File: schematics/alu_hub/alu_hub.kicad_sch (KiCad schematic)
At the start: 23 parts, among them U1 74LS574, U10 74LS02, U2 74LS245, U3 74LS02, U4 74LS181, U5 74LS181, U6 74LS574, U7 74LS245, U8 74LS245, U9 74LS02

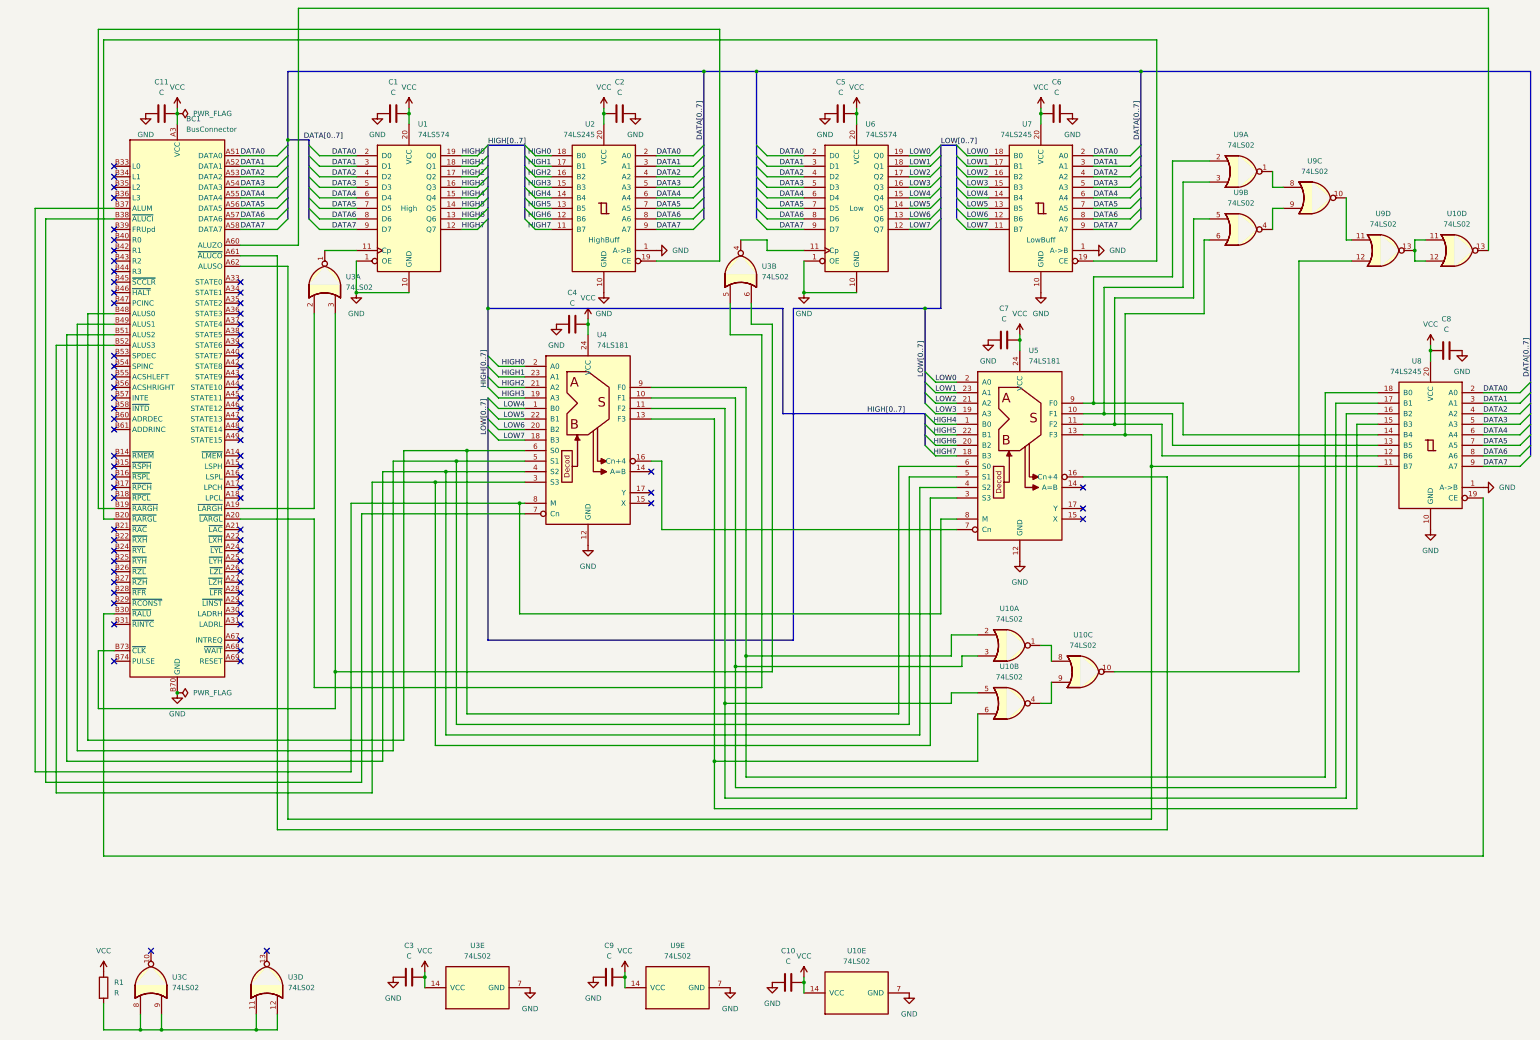
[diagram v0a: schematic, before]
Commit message: Add test points
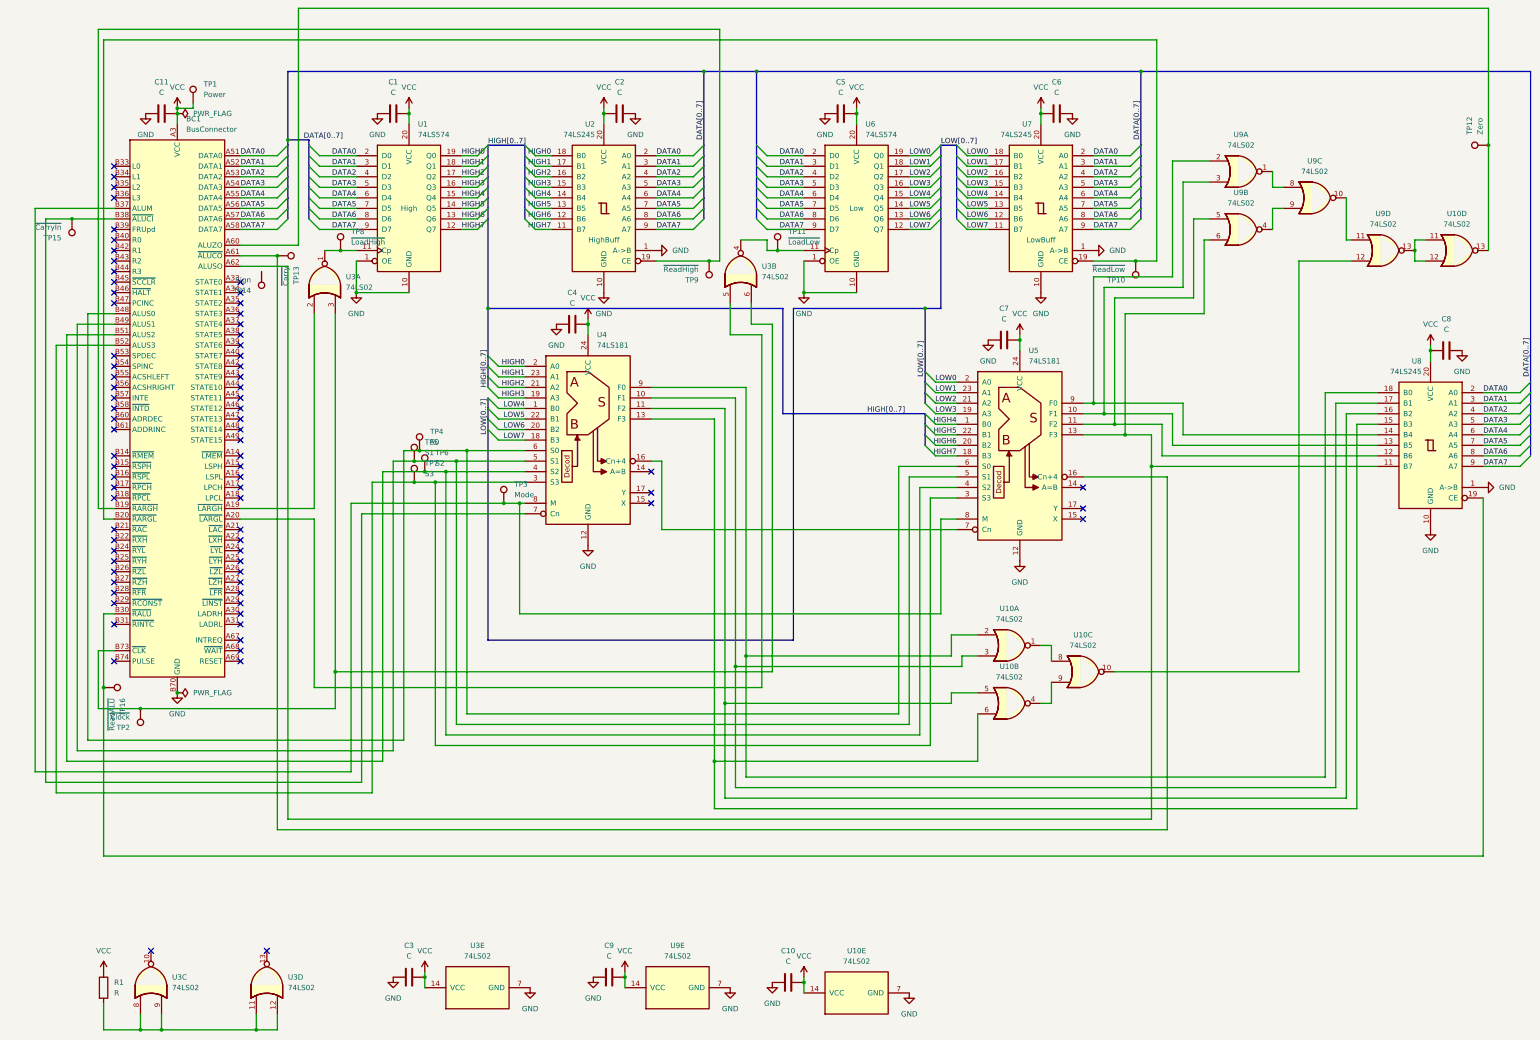
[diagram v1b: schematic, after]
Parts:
- added TP1: Power, Connector_Pin:Pin_D1.0mm_L10.0mm, symbol Connector:TestPoint
- added TP10: ~{ReadLow}, Connector_Pin:Pin_D1.0mm_L10.0mm, symbol Connector:TestPoint
- added TP11: ~{LoadLow}, Connector_Pin:Pin_D1.0mm_L10.0mm, symbol Connector:TestPoint
- added TP12: Zero, Connector_Pin:Pin_D1.0mm_L10.0mm, symbol Connector:TestPoint
- added TP13: ~{Carry}, Connector_Pin:Pin_D1.0mm_L10.0mm, symbol Connector:TestPoint
- added TP14: Sign, Connector_Pin:Pin_D1.0mm_L10.0mm, symbol Connector:TestPoint
- added TP15: ~{CarryIn}, Connector_Pin:Pin_D1.0mm_L10.0mm, symbol Connector:TestPoint
- added TP16: ~{ReadALU}, Connector_Pin:Pin_D1.0mm_L10.0mm, symbol Connector:TestPoint
- added TP2: ~{Clock}, Connector_Pin:Pin_D1.0mm_L10.0mm, symbol Connector:TestPoint
- added TP3: Mode, Connector_Pin:Pin_D1.0mm_L10.0mm, symbol Connector:TestPoint
- added TP4: S0, Connector_Pin:Pin_D1.0mm_L10.0mm, symbol Connector:TestPoint
- added TP5: S1, Connector_Pin:Pin_D1.0mm_L10.0mm, symbol Connector:TestPoint
- added TP6: S2, Connector_Pin:Pin_D1.0mm_L10.0mm, symbol Connector:TestPoint
- added TP7: S3, Connector_Pin:Pin_D1.0mm_L10.0mm, symbol Connector:TestPoint
- added TP8: ~{LoadHigh}, Connector_Pin:Pin_D1.0mm_L10.0mm, symbol Connector:TestPoint
- added TP9: ~{ReadHigh}, Connector_Pin:Pin_D1.0mm_L10.0mm, symbol Connector:TestPoint
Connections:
- net VCC: now also TP1.1
- net at U3.4, U6.11 (Cp): now also TP11.1
- net at BC1.B73 (~{CLK}), U3.3, U3.6: now also TP2.1
- net at BC1.B30 (~{RALU}), U8.19 (CE): now also TP16.1
- net at BC1.B20 (~{RARGL}), U7.19 (CE): now also TP10.1
- net at BC1.A60 (ALUZO), U10.13: now also TP12.1
- net at BC1.A61 (~{ALUCO}), U5.16 (Cn+4): now also TP13.1
- net at BC1.B19 (~{RARGH}), U2.19 (CE): now also TP9.1
- net at BC1.B37 (ALUM), U4.8 (M), U5.8 (M): now also TP3.1
- net at BC1.B38 (~{ALUCI}), U4.7 (Cn): now also TP15.1
- net at BC1.B48 (ALUS0), U4.6 (S0), U5.6 (S0): now also TP4.1
- net at BC1.B49 (ALUS1), U4.5 (S1), U5.5 (S1): now also TP5.1
- net at BC1.B51 (ALUS2), U4.4 (S2), U5.4 (S2): now also TP6.1
- net at BC1.B52 (ALUS3), U4.3 (S3), U5.3 (S3): now also TP7.1
- net at U1.11 (Cp), U3.1: now also TP8.1

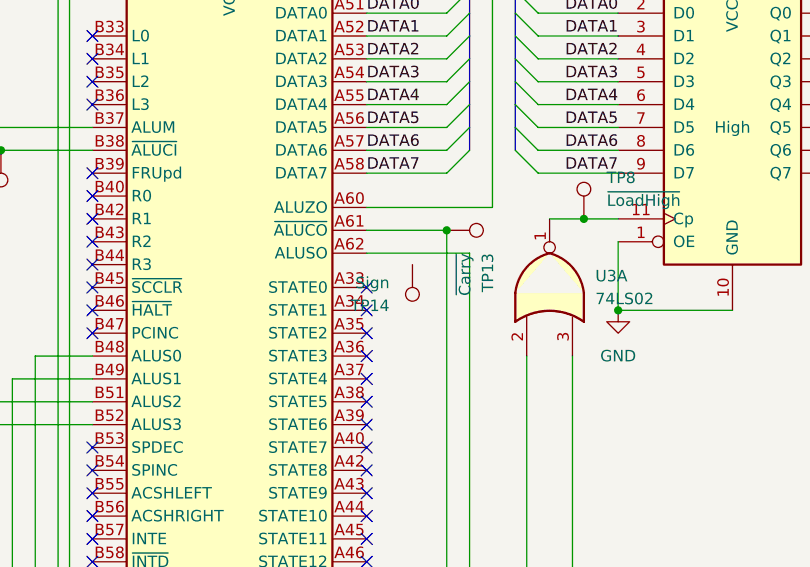
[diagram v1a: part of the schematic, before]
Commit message: Add test points in Core 1
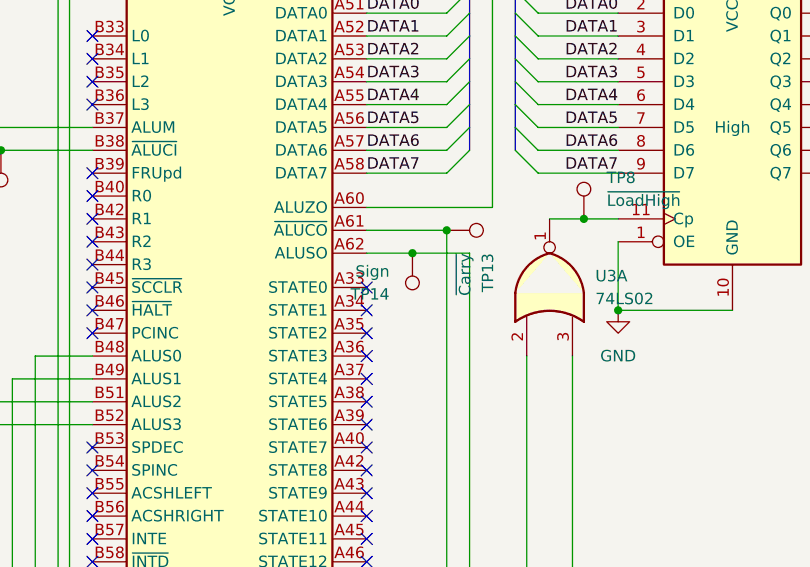
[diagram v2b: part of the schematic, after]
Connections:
- net at BC1.A62 (ALUSO), U5.13 (F3), U8.11 (B7)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: now also TP14.1
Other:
- moved on the sheet: TP14
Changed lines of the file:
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@@
 	)
 	(junction
+		(at 80.01 90.17)
+		(diameter 0)
+		(color 0 0 0 0)
+	)
+	(junction
 		(at 292.1 43.18)
 		(diameter 0)
@@
 		)
 	)
+	(wire
+		(pts
+			(xy 80.01 90.17) (xy 74.93 90.17)
+		)
+		(stroke
+			(width 0)
+			(type default)
+		)
+	)
 	(bus
 		(pts
@@
 	(wire
 		(pts
-			(xy 86.36 90.17) (xy 74.93 90.17)
+			(xy 86.36 90.17) (xy 80.01 90.17)
 		)
 		(stroke
@@
 	(symbol
 		(lib_id "Connector:TestPoint")
-		(at 80.01 91.44 180)
+		(at 80.01 90.17 180)
 		(unit 1)
 		(exclude_from_sim no)
@@
 		(dnp no)
 		(property "Reference" "TP14"
-			(at 77.47 96.0121 0)
+			(at 77.47 94.7421 0)
 			(effects
 				(font
@@
 		)
 		(property "Value" "Sign"
-			(at 77.47 93.4721 0)
+			(at 77.47 92.2021 0)
 			(effects
 				(font
@@
 		)
 		(property "Footprint" "Connector_Pin:Pin_D1.0mm_L10.0mm"
-			(at 74.93 91.44 0)
+			(at 74.93 90.17 0)
 			(effects
 				(font
@@
 		)
 		(property "Datasheet" "~"
-			(at 74.93 91.44 0)
+			(at 74.93 90.17 0)
 			(effects
 				(font
@@
 		)
 		(property "Description" "test point"
-			(at 80.01 91.44 0)
+			(at 80.01 90.17 0)
 			(effects
 				(font
